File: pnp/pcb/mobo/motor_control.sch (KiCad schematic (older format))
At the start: 37 parts, among them J1 X_MOTOR, J2 Y_MOTOR1, J3 Z_MOTOR, J37 P_MOTOR, J38 C_MOTOR, J4 R_MOTOR, J48 Y_MOTOR2

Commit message: fixed fault pin on stepper drivers
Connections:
- wire segments 168 -> 174
- no-connect marks 6 -> 0
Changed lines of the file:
@@
 Wire Wire Line
 	1900 6150 1450 6150
-NoConn ~ 1900 5950
-NoConn ~ 1550 3900
-NoConn ~ 1950 1650
 $Comp
 L Driver_Motor:Pololu_Breakout_DRV8825 A6
@@
 Wire Wire Line
 	4900 6150 4450 6150
-NoConn ~ 4900 5950
-NoConn ~ 5000 3900
-NoConn ~ 4850 1700
 $Comp
 L Device:CP C4
@@
 Wire Wire Line
 	5650 2000 5750 2000
+Wire Wire Line
+	1550 3900 1100 3900
+Connection ~ 1100 3900
+Wire Wire Line
+	1950 1650 1500 1650
+Connection ~ 1500 1650
+Wire Wire Line
+	1900 5950 1450 5950
+Connection ~ 1450 5950
+Wire Wire Line
+	4900 5950 4450 5950
+Connection ~ 4450 5950
+Wire Wire Line
+	5000 3900 4550 3900
+Connection ~ 4550 3900
+Wire Wire Line
+	4850 1700 4400 1700
+Connection ~ 4400 1700
 $EndSCHEMATC

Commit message: updating M0/1/2 pins on stepper driver headers to work for SPI. jumper config not yet finished
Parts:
- removed JP1, JP22, JP25, JP28, JP4, JP7: M0, Jumper:SolderJumper-2_P1.3mm_Open_RoundedPad1.0x1.5mm, symbol Device:Jumper_NO_Small
- removed JP2, JP23, JP26, JP29, JP5, JP8: M1, Jumper:SolderJumper-2_P1.3mm_Open_RoundedPad1.0x1.5mm, symbol Device:Jumper_NO_Small
- removed JP24, JP27, JP3, JP30, JP6, JP9: M2, Jumper:SolderJumper-2_P1.3mm_Open_RoundedPad1.0x1.5mm, symbol Device:Jumper_NO_Small
- added JP? (x16): SolderJumper_3_Open, symbol Jumper:SolderJumper_3_Open
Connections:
- net labels added: C_CS, C_MS0_MOSI, C_MS1_SCK, C_MS2_CS, C_RST_MISO, MISO, MOSI, P_CS, P_MS0_MOSI, P_MS1_SCK, P_MS2_CS, P_RST_MISO, R_CS, R_MS0_MOSI, R_MS1_SCK, R_MS2_CS, R_RST_MISO, SCK, X_CS, X_MS0_MOSI, X_MS1_SCK, X_MS2_CS, X_RST_MISO, Y_CS, Y_MS0_MOSI, Y_MS1_SCK, Y_MS2_CS, Y_RST_MISO, Z_CS, Z_MS0_MOSI, Z_MS1_SCK, Z_MS2_CS, Z_RST_MISO
- wire segments 174 -> 165
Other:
- note added: "MAKE SURE TO SWITCH TO PIN JUMPERS YOU DINGUS\n"
- moved on the sheet: A1, A4, A5, A6, J1, J37, J38, J4

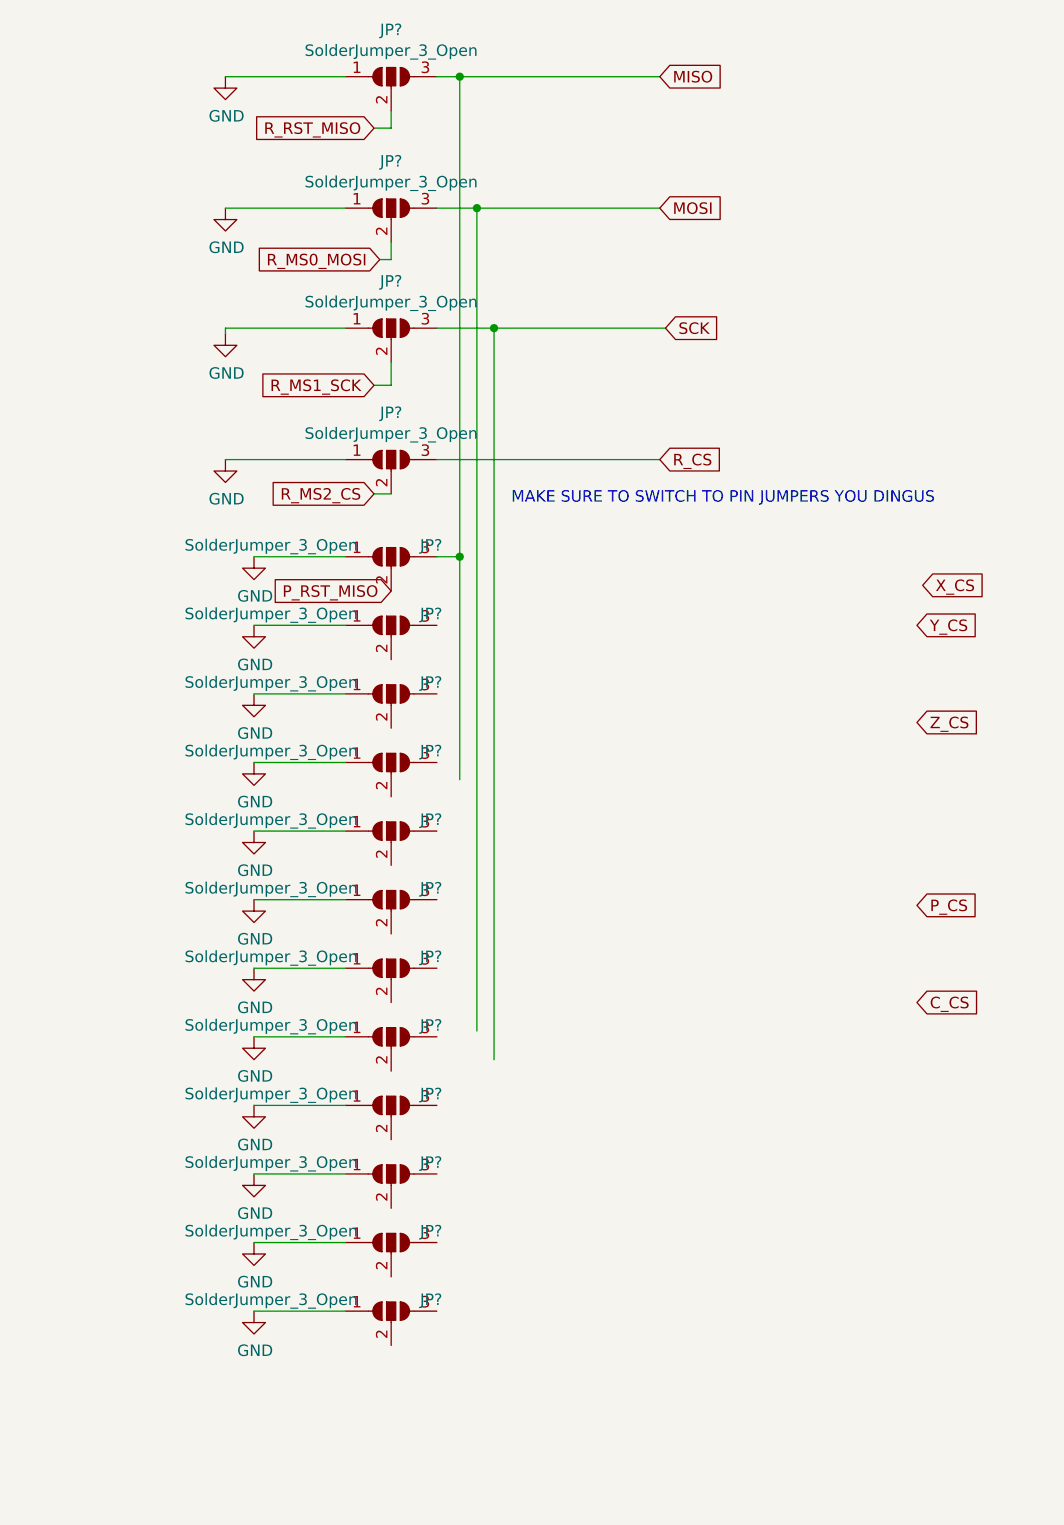
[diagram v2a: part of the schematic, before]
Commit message: all SPI jumpers for the stepper motor drivers are wired up in the schematic
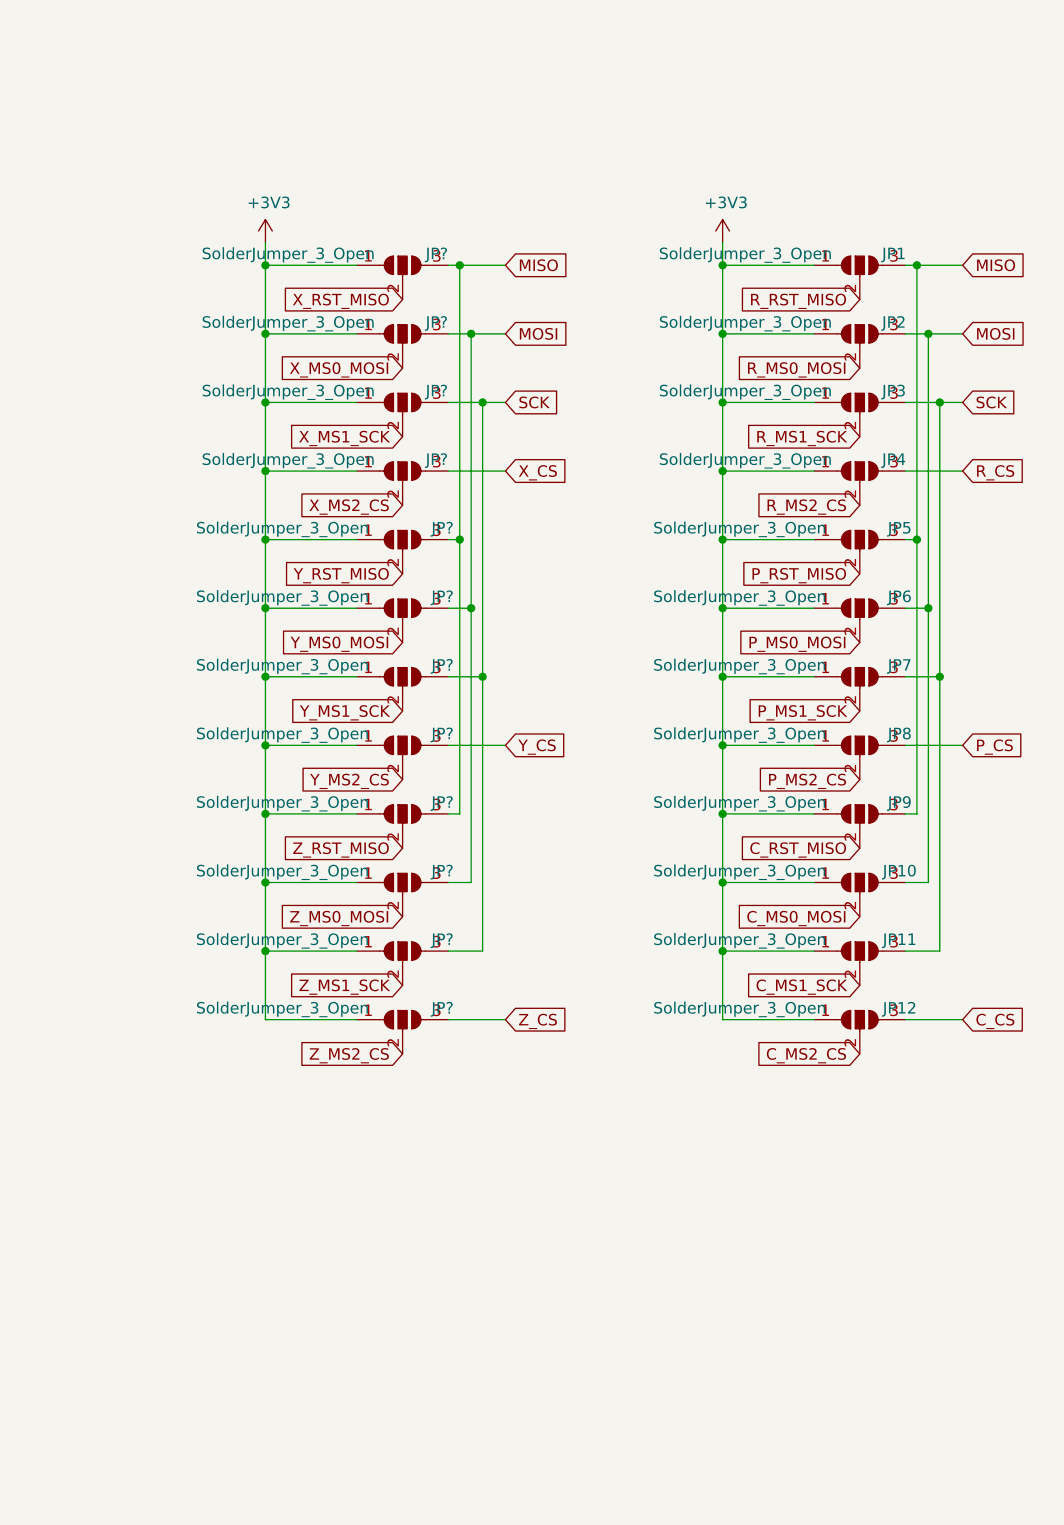
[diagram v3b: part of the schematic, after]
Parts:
- removed JP? (x4): SolderJumper_3_Open, symbol Jumper:SolderJumper_3_Open
- added JP? (x12): SolderJumper_3_Open, Connector_PinHeader_2.54mm:PinHeader_1x03_P2.54mm_Vertical, symbol Jumper:SolderJumper_3_Open
- JP1, JP10, JP11, JP12, JP2, JP3, JP4, JP5, JP6, JP7, JP8, JP9: renamed from JP?; footprint (none) -> Connector_PinHeader_2.54mm:PinHeader_1x03_P2.54mm_Vertical
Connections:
- net +3V3: now also JP1.1 (A), JP10.1 (A), JP11.1 (A), JP12.1 (A), JP2.1 (A), JP3.1 (A), JP4.1 (A), JP5.1 (A), JP6.1 (A), JP7.1 (A), JP8.1 (A), JP9.1 (A), JP?.1 (A), JP?.1 (A), JP?.1 (A), JP?.1 (A), JP?.1 (A), JP?.1 (A), JP?.1 (A), JP?.1 (A), JP?.1 (A), JP?.1 (A), JP?.1 (A), JP?.1 (A)
- net C_CS: now also JP12.3 (B)
- net C_MS0_MOSI: now also JP10.2 (C)
- net C_MS1_SCK: now also JP11.2 (C)
- net C_MS2_CS: now also JP12.2 (C)
- net C_RST_MISO: now also JP9.2 (C)
- net GND: no longer JP1.1 (A), JP10.1 (A), JP11.1 (A), JP12.1 (A), JP2.1 (A), JP3.1 (A), JP4.1 (A), JP5.1 (A), JP6.1 (A), JP7.1 (A), JP8.1 (A), JP9.1 (A)
- net MISO: now also JP9.3 (B), JP?.3 (B), JP?.3 (B), JP?.3 (B)
- net MOSI: now also JP10.3 (B), JP6.3 (B), JP?.3 (B), JP?.3 (B), JP?.3 (B)
- net P_CS: now also JP8.3 (B)
- net P_MS0_MOSI: now also JP6.2 (C)
- net P_MS1_SCK: now also JP7.2 (C)
- net P_MS2_CS: now also JP8.2 (C)
- net SCK: now also JP11.3 (B), JP7.3 (B), JP?.3 (B), JP?.3 (B), JP?.3 (B)
- net X_CS: now also JP?.3 (B)
- net X_MS0_MOSI: now also JP?.2 (C)
- net X_MS1_SCK: now also JP?.2 (C)
- net X_MS2_CS: now also JP?.2 (C)
- net X_RST_MISO: now also JP?.2 (C)
- net Y_CS: now also JP?.3 (B)
- net Y_MS0_MOSI: now also JP?.2 (C)
- net Y_MS1_SCK: now also JP?.2 (C)
- net Y_MS2_CS: now also JP?.2 (C)
- net Y_RST_MISO: now also JP?.2 (C)
- net Z_CS: now also JP?.3 (B)
- net Z_MS0_MOSI: now also JP?.2 (C)
- net Z_MS1_SCK: now also JP?.2 (C)
- net Z_MS2_CS: now also JP?.2 (C)
- net Z_RST_MISO: now also JP?.2 (C)
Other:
- note removed: "MAKE SURE TO SWITCH TO PIN JUMPERS YOU DINGUS\n"
- moved on the sheet: JP1, JP10, JP11, JP12, JP2, JP3, JP4, JP5, JP6, JP7, JP8, JP9

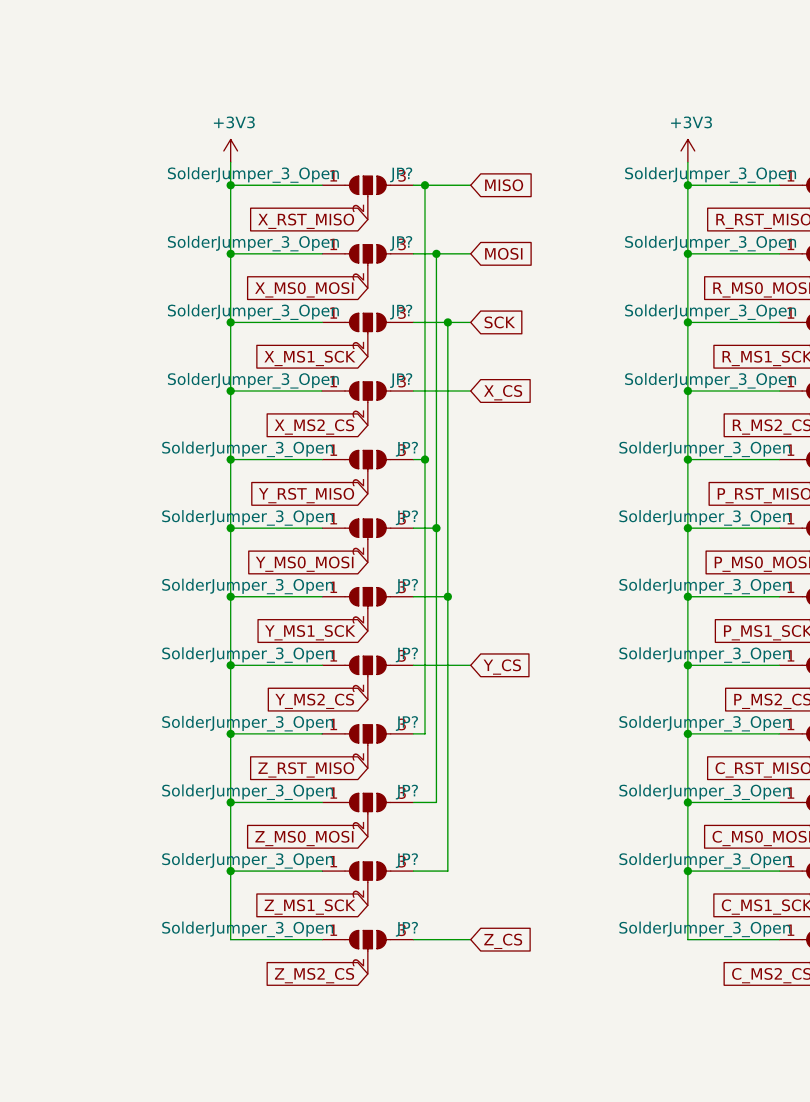
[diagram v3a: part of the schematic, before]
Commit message: improved main sch layout a bit, updated fet footprint to TO-252-2
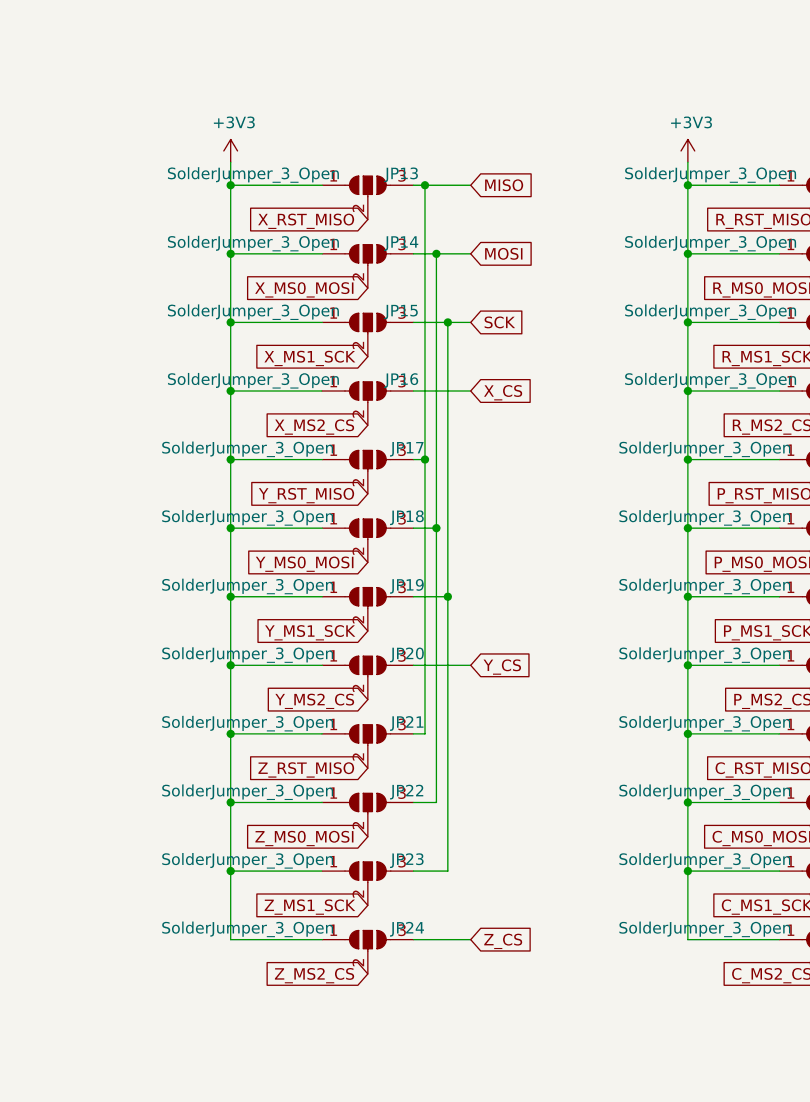
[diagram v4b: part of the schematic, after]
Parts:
- gave numbers to parts that had none: 12
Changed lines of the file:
@@
 	10100 4750 10350 4750
 $Comp
-L Jumper:SolderJumper_3_Open JP?
+L Jumper:SolderJumper_3_Open JP13
 U 1 1 5F9E5B59
 P 7900 1450
-F 0 "JP?" H 8050 1500 50  0000 C CNN
+F 0 "JP13" H 8050 1500 50  0000 C CNN
 F 1 "SolderJumper_3_Open" H 7400 1500 50  0000 C CNN
 F 2 "Connector_PinHeader_2.54mm:PinHeader_1x03_P2.54mm_Vertical" H 7900 1450 50  0001 C CNN
@@
 SCK
 $Comp
-L Jumper:SolderJumper_3_Open JP?
+L Jumper:SolderJumper_3_Open JP14
 U 1 1 5F9E5B74
 P 7900 1750
-F 0 "JP?" H 8050 1800 50  0000 C CNN
+F 0 "JP14" H 8050 1800 50  0000 C CNN
 F 1 "SolderJumper_3_Open" H 7400 1800 50  0000 C CNN
 F 2 "Connector_PinHeader_2.54mm:PinHeader_1x03_P2.54mm_Vertical" H 7900 1750 50  0001 C CNN
@@
 $EndComp
 $Comp
-L Jumper:SolderJumper_3_Open JP?
+L Jumper:SolderJumper_3_Open JP15
 U 1 1 5F9E5B8A
 P 7900 2050
-F 0 "JP?" H 8050 2100 50  0000 C CNN
+F 0 "JP15" H 8050 2100 50  0000 C CNN
 F 1 "SolderJumper_3_Open" H 7400 2100 50  0000 C CNN
 F 2 "Connector_PinHeader_2.54mm:PinHeader_1x03_P2.54mm_Vertical" H 7900 2050 50  0001 C CNN
@@
 $EndComp
 $Comp
-L Jumper:SolderJumper_3_Open JP?
+L Jumper:SolderJumper_3_Open JP16
 U 1 1 5F9E5B9F
 P 7900 2350
-F 0 "JP?" H 8050 2400 50  0000 C CNN
+F 0 "JP16" H 8050 2400 50  0000 C CNN
 F 1 "SolderJumper_3_Open" H 7400 2400 50  0000 C CNN
 F 2 "Connector_PinHeader_2.54mm:PinHeader_1x03_P2.54mm_Vertical" H 7900 2350 50  0001 C CNN
@@
 $EndComp
 $Comp
-L Jumper:SolderJumper_3_Open JP?
+L Jumper:SolderJumper_3_Open JP17
 U 1 1 5F9E5BB4
 P 7900 2650
-F 0 "JP?" H 8075 2700 50  0000 C CNN
+F 0 "JP17" H 8075 2700 50  0000 C CNN
 F 1 "SolderJumper_3_Open" H 7375 2700 50  0000 C CNN
 F 2 "Connector_PinHeader_2.54mm:PinHeader_1x03_P2.54mm_Vertical" H 7900 2650 50  0001 C CNN
@@
 $EndComp
 $Comp
-L Jumper:SolderJumper_3_Open JP?
+L Jumper:SolderJumper_3_Open JP18
 U 1 1 5F9E5BC9
 P 7900 2950
-F 0 "JP?" H 8075 3000 50  0000 C CNN
+F 0 "JP18" H 8075 3000 50  0000 C CNN
 F 1 "SolderJumper_3_Open" H 7375 3000 50  0000 C CNN
 F 2 "Connector_PinHeader_2.54mm:PinHeader_1x03_P2.54mm_Vertical" H 7900 2950 50  0001 C CNN
@@
 $EndComp
 $Comp
-L Jumper:SolderJumper_3_Open JP?
+L Jumper:SolderJumper_3_Open JP20
 U 1 1 5F9E5BF1
 P 7900 3550
-F 0 "JP?" H 8075 3600 50  0000 C CNN
+F 0 "JP20" H 8075 3600 50  0000 C CNN
 F 1 "SolderJumper_3_Open" H 7375 3600 50  0000 C CNN
 F 2 "Connector_PinHeader_2.54mm:PinHeader_1x03_P2.54mm_Vertical" H 7900 3550 50  0001 C CNN
@@
 $EndComp
 $Comp
-L Jumper:SolderJumper_3_Open JP?
+L Jumper:SolderJumper_3_Open JP21
 U 1 1 5F9E5C05
 P 7900 3850
-F 0 "JP?" H 8075 3900 50  0000 C CNN
+F 0 "JP21" H 8075 3900 50  0000 C CNN
 F 1 "SolderJumper_3_Open" H 7375 3900 50  0000 C CNN
 F 2 "Connector_PinHeader_2.54mm:PinHeader_1x03_P2.54mm_Vertical" H 7900 3850 50  0001 C CNN
@@
 $EndComp
 $Comp
-L Jumper:SolderJumper_3_Open JP?
+L Jumper:SolderJumper_3_Open JP22
 U 1 1 5F9E5C19
 P 7900 4150
-F 0 "JP?" H 8075 4200 50  0000 C CNN
+F 0 "JP22" H 8075 4200 50  0000 C CNN
 F 1 "SolderJumper_3_Open" H 7375 4200 50  0000 C CNN
 F 2 "Connector_PinHeader_2.54mm:PinHeader_1x03_P2.54mm_Vertical" H 7900 4150 50  0001 C CNN
@@
 $EndComp
 $Comp
-L Jumper:SolderJumper_3_Open JP?
+L Jumper:SolderJumper_3_Open JP23
 U 1 1 5F9E5C2D
 P 7900 4450
-F 0 "JP?" H 8075 4500 50  0000 C CNN
+F 0 "JP23" H 8075 4500 50  0000 C CNN
 F 1 "SolderJumper_3_Open" H 7375 4500 50  0000 C CNN
 F 2 "Connector_PinHeader_2.54mm:PinHeader_1x03_P2.54mm_Vertical" H 7900 4450 50  0001 C CNN
@@
 $EndComp
 $Comp
-L Jumper:SolderJumper_3_Open JP?
+L Jumper:SolderJumper_3_Open JP24
 U 1 1 5F9E5C41
 P 7900 4750
-F 0 "JP?" H 8075 4800 50  0000 C CNN
+F 0 "JP24" H 8075 4800 50  0000 C CNN
 F 1 "SolderJumper_3_Open" H 7375 4800 50  0000 C CNN
 F 2 "Connector_PinHeader_2.54mm:PinHeader_1x03_P2.54mm_Vertical" H 7900 4750 50  0001 C CNN
@@
 	8100 4750 8350 4750
 $Comp
-L Jumper:SolderJumper_3_Open JP?
+L Jumper:SolderJumper_3_Open JP19
 U 1 1 5F9E5BDD
 P 7900 3250
-F 0 "JP?" H 8075 3300 50  0000 C CNN
+F 0 "JP19" H 8075 3300 50  0000 C CNN
 F 1 "SolderJumper_3_Open" H 7375 3300 50  0000 C CNN
 F 2 "Connector_PinHeader_2.54mm:PinHeader_1x03_P2.54mm_Vertical" H 7900 3250 50  0001 C CNN
@@
 Z_MS2_CS
 $Comp
-L power:+3V3 #PWR?
+L power:+3V3 #PWR0125
 U 1 1 5FA03C15
 P 7300 1350
-F 0 "#PWR?" H 7300 1200 50  0001 C CNN
+F 0 "#PWR0125" H 7300 1200 50  0001 C CNN
 F 1 "+3V3" H 7315 1523 50  0000 C CNN
 F 2 "" H 7300 1350 50  0001 C CNN
@@
 	9300 2350 9300 2050
 $Comp
-L power:+3V3 #PWR?
+L power:+3V3 #PWR0187
 U 1 1 5FA5CA7A
 P 9300 1350
-F 0 "#PWR?" H 9300 1200 50  0001 C CNN
+F 0 "#PWR0187" H 9300 1200 50  0001 C CNN
 F 1 "+3V3" H 9315 1523 50  0000 C CNN
 F 2 "" H 9300 1350 50  0001 C CNN
